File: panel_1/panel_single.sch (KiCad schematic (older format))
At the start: 6 parts

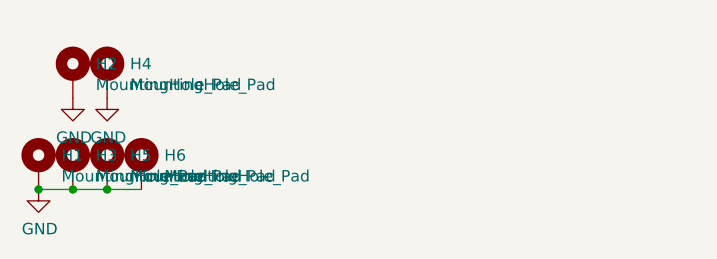
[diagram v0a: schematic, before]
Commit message: :bug: Fix panel single (better clearance for LEDs & switch)
same
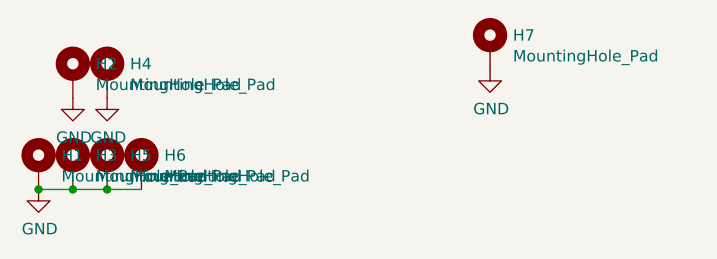
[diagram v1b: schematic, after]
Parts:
- added H7: MountingHole_Pad, MountingHole:MountingHole_6mm_Pad, symbol Mechanical:MountingHole_Pad
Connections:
- net GND: now also H7.1
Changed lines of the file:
@@
 EESchema Schematic File Version 4
-EELAYER 29 0
+EELAYER 30 0
 EELAYER END
 $Descr A4 11693 8268
@@
 Wire Wire Line
 	2500 2550 2650 2550
+$Comp
+L Mechanical:MountingHole_Pad H7
+U 1 1 5F06390A
+P 4175 1925
+F 0 "H7" H 4275 1974 50  0000 L CNN
+F 1 "MountingHole_Pad" H 4275 1883 50  0000 L CNN
+F 2 "MountingHole:MountingHole_6mm_Pad" H 4175 1925 50  0001 C CNN
+F 3 "~" H 4175 1925 50  0001 C CNN
+	1    4175 1925
+	1    0    0    -1
+$EndComp
+$Comp
+L power:GND #PWR0104
+U 1 1 5F063910
+P 4175 2025
+F 0 "#PWR0104" H 4175 1775 50  0001 C CNN
+F 1 "GND" H 4180 1852 50  0000 C CNN
+F 2 "" H 4175 2025 50  0001 C CNN
+F 3 "" H 4175 2025 50  0001 C CNN
+	1    4175 2025
+	1    0    0    -1
+$EndComp
 $EndSCHEMATC
